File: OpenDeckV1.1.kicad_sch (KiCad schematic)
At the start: 0 parts

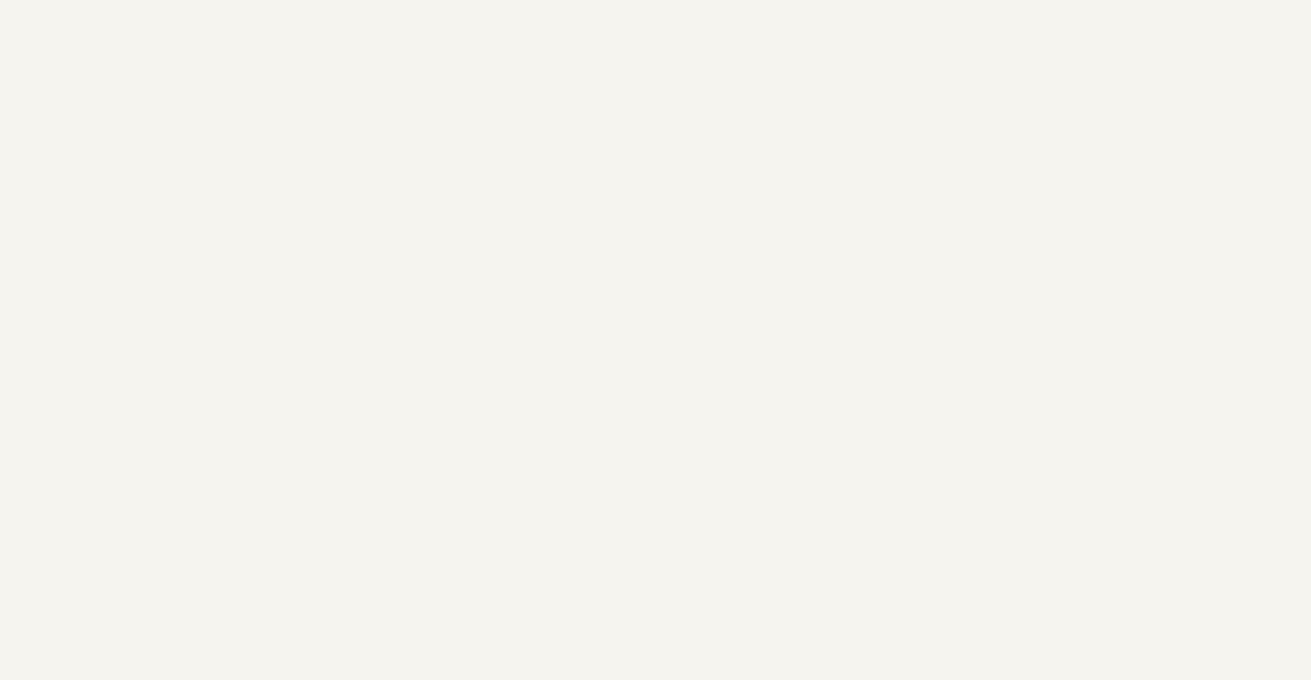
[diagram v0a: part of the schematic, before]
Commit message: imported DRV2605L haptic motor driver circuit
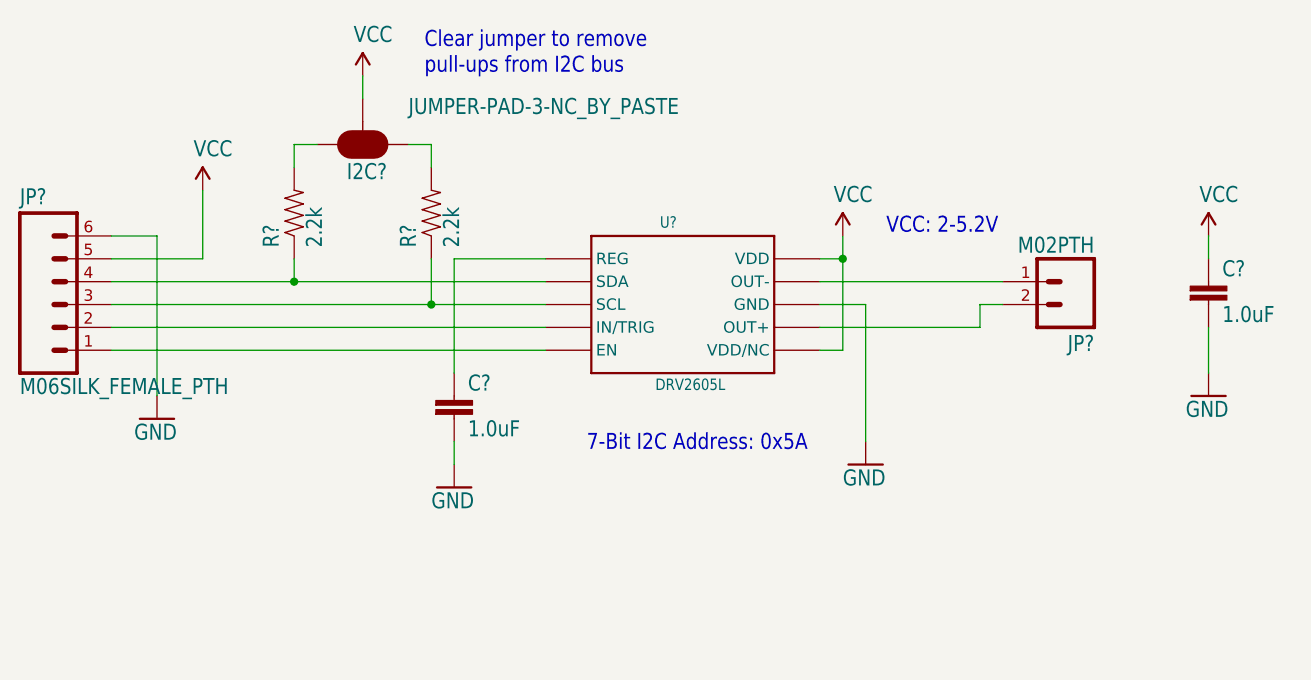
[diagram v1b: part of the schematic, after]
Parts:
- added C? (x2): 1.0uF, OpenDeckV1.1:0402-CAP, symbol OpenDeckV1.1-eagle-import:1.0UF-16V-10%(0402)
- added I2C?: JUMPER-PAD-3-NC_BY_PASTE, OpenDeckV1.1:PAD-JUMPER-3-NC_BY_PASTE_YES_SILK_FULL_BOX, symbol OpenDeckV1.1-eagle-import:JUMPER-PAD-3-NC_BY_PASTE
- added JP?: M02PTH, OpenDeckV1.1:1X02, symbol OpenDeckV1.1-eagle-import:M02PTH
- added JP?: M06SILK_FEMALE_PTH, OpenDeckV1.1:1X06, symbol OpenDeckV1.1-eagle-import:M06SILK_FEMALE_PTH
- added R? (x2): 2.2k, OpenDeckV1.1:0603-RES, symbol OpenDeckV1.1-eagle-import:2.2KOHM-1/10W-1%(0603)
- added U?: DRV2605L, OpenDeckV1.1:VSSOP-10, symbol OpenDeckV1.1-eagle-import:DRV2605L
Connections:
- new net: C?.1, U?.P$1 (REG)
- new net: JP?.3, R?.1, U?.P$2 (SCL)
- new net: JP?.4, R?.1, U?.P$3 (SDA)
- new net: JP?.2, U?.P$4 (IN/TRIG)
- new net: JP?.1, U?.P$5 (EN)
- new net: JP?.2, U?.P$7 (OUT+)
- new net: JP?.1, U?.P$9 (OUT-)
- new net: I2C?.1, R?.2
- new net: I2C?.3, R?.2
- new net GND: C?.2, C?.2, JP?.6, U?.P$8 (GND)
- new net VCC: C?.1, I2C?.2, JP?.5, U?.P$10 (VDD), U?.P$6 (VDD/NC)
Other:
- note added: "7-Bit I2C Address: 0x5A"
- note added: "Clear jumper to remove pull-ups from I2C bus"
- note added: "VCC: 2-5.2V"

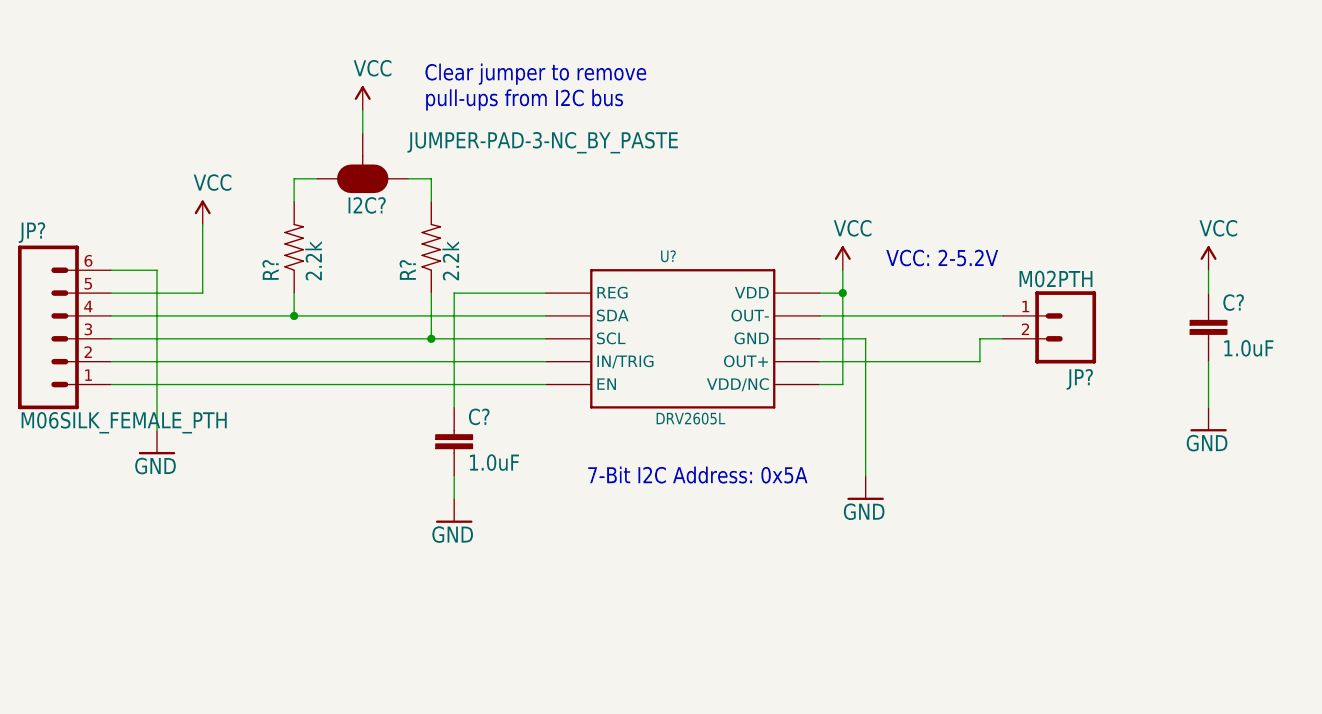
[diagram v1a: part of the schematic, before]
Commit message: copied in sparkfun DRV2605L haptic motor driver circuit
from sparkfun github
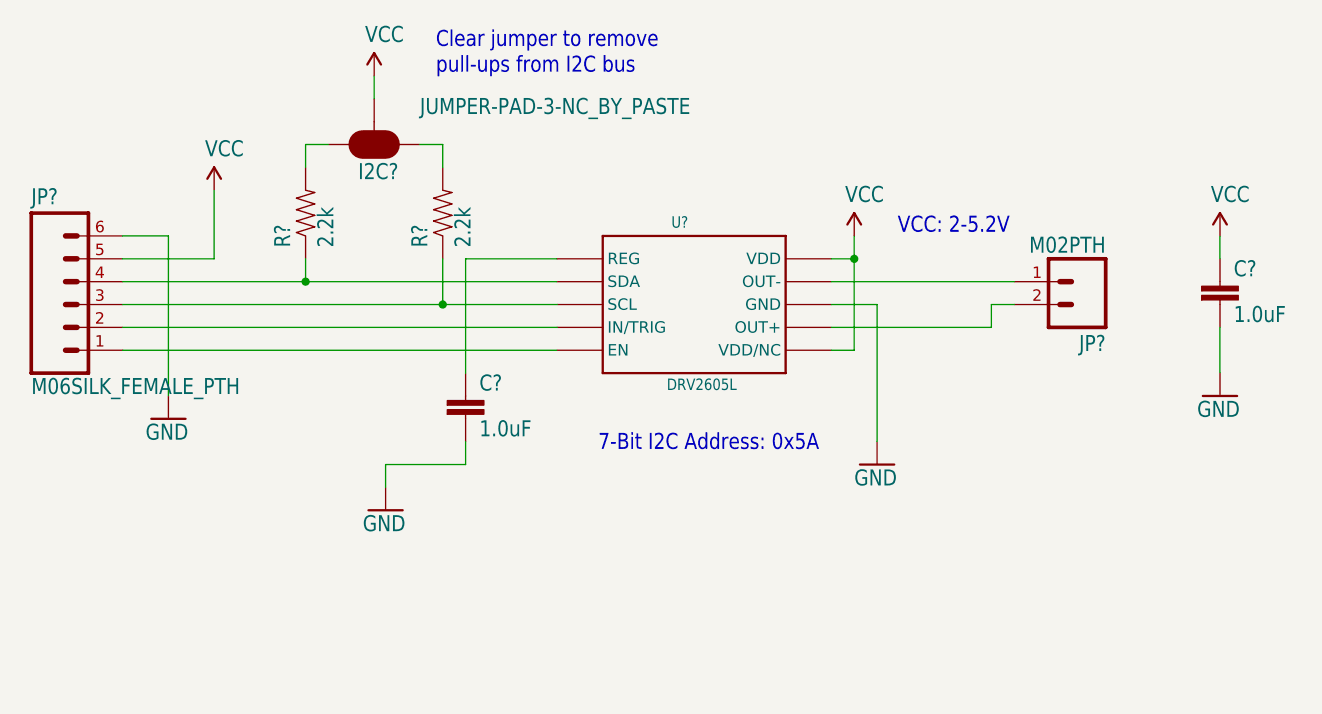
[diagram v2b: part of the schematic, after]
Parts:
- removed C? (x2): 1.0uF, OpenDeckV1.1:0402-CAP, symbol OpenDeckV1.1-eagle-import:1.0UF-16V-10%(0402)
- removed I2C?: JUMPER-PAD-3-NC_BY_PASTE, OpenDeckV1.1:PAD-JUMPER-3-NC_BY_PASTE_YES_SILK_FULL_BOX, symbol OpenDeckV1.1-eagle-import:JUMPER-PAD-3-NC_BY_PASTE
- removed JP?: M02PTH, OpenDeckV1.1:1X02, symbol OpenDeckV1.1-eagle-import:M02PTH
- removed JP?: M06SILK_FEMALE_PTH, OpenDeckV1.1:1X06, symbol OpenDeckV1.1-eagle-import:M06SILK_FEMALE_PTH
- removed R? (x2): 2.2k, OpenDeckV1.1:0603-RES, symbol OpenDeckV1.1-eagle-import:2.2KOHM-1/10W-1%(0603)
- removed U?: DRV2605L, OpenDeckV1.1:VSSOP-10, symbol OpenDeckV1.1-eagle-import:DRV2605L
- added C? (x2): 1.0uF, OpenDeckV1.0:0402-CAP, symbol OpenDeckV1.0-eagle-import:1.0UF-16V-10%(0402)
- added I2C?: JUMPER-PAD-3-NC_BY_PASTE, OpenDeckV1.0:PAD-JUMPER-3-NC_BY_PASTE_YES_SILK_FULL_BOX, symbol OpenDeckV1.0-eagle-import:JUMPER-PAD-3-NC_BY_PASTE
- added JP?: M06SILK_FEMALE_PTH, OpenDeckV1.0:1X06, symbol OpenDeckV1.0-eagle-import:M06SILK_FEMALE_PTH
- added JP?: M02PTH, OpenDeckV1.0:1X02, symbol OpenDeckV1.0-eagle-import:M02PTH
- added R? (x2): 2.2k, OpenDeckV1.0:0603-RES, symbol OpenDeckV1.0-eagle-import:2.2KOHM-1/10W-1%(0603)
- added U?: DRV2605L, OpenDeckV1.0:VSSOP-10, symbol OpenDeckV1.0-eagle-import:DRV2605L
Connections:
- net GND: now also C?.2, C?.2, JP?.6, U?.P$8 (GND)
- net VCC: now also C?.1, I2C?.2, JP?.5, U?.P$10 (VDD), U?.P$6 (VDD/NC)
- new net: C?.1, U?.P$1 (REG)
- new net: JP?.4, R?.1, U?.P$3 (SDA)
- new net: I2C?.3, R?.2
- new net: I2C?.1, R?.2
- new net: JP?.3, R?.1, U?.P$2 (SCL)
- new net: JP?.1, U?.P$5 (EN)
- new net: JP?.2, U?.P$4 (IN/TRIG)
- new net: JP?.1, U?.P$9 (OUT-)
- new net: JP?.2, U?.P$7 (OUT+)
